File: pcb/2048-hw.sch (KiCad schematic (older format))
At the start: 98 parts, among them J1 UJC-HP-3-SMT-TR, J2 Battery, J3 SWD, SW1 SW_SPDT, SW2 PUSH_A, SW3 PUSH_B, U1 STM32F303K8Tx, U2 MCP73831-2-OT, U3 AP2210N-3.3TRG1, U4 PSP_1000_JSTK, U5 LMV339, Y1 ECS-80-12-30Q-DS-TR

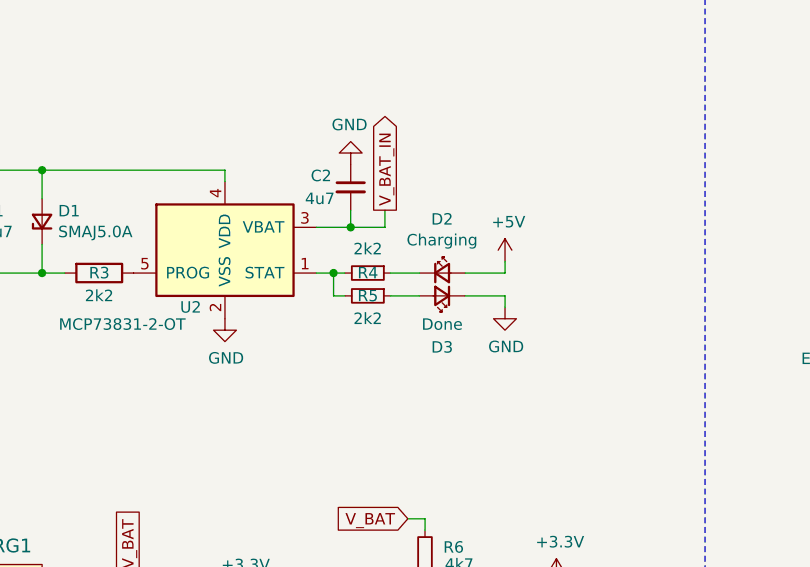
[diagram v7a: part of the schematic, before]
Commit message: Shink down PCB dimensions
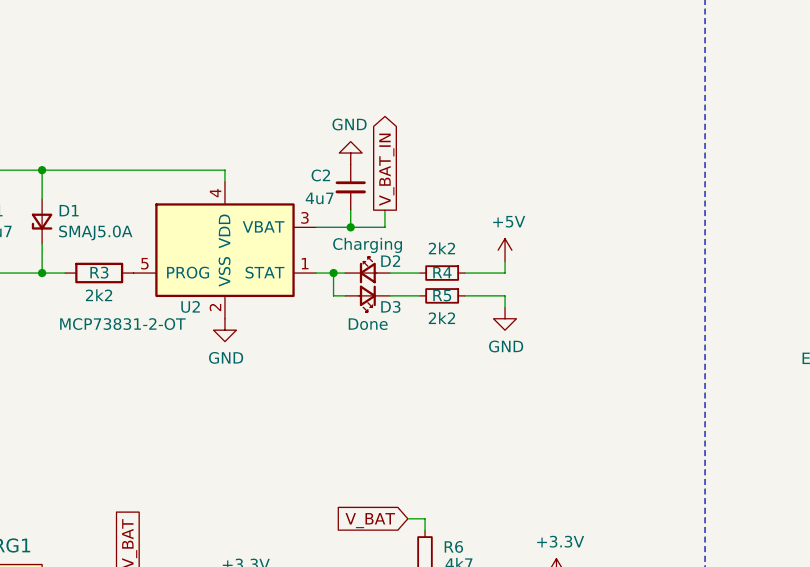
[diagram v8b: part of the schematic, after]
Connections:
- net +5V: now also R4.1; no longer D2.2 (A)
- net GND: now also R5.1; no longer D3.1 (K)
- net at D2.1 (K): now also D3.2 (A), U2.1 (STAT); no longer R4.1
- new net: D2.2 (A), R4.2
- new net: D3.1 (K), R5.2
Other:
- moved on the sheet: D2, D3, R4, R5
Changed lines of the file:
@@
 L Device:LED_Small D2
 U 1 1 5FF0DDA7
-P 5475 1800
-F 0 "D2" H 5475 2035 50  0000 C CNN
-F 1 "Charging" H 5475 1944 50  0000 C CNN
-F 2 "LED_SMD:LED_0603_1608Metric_Pad1.05x0.95mm_HandSolder" V 5475 1800 50  0001 C CNN
-F 3 "~" V 5475 1800 50  0001 C CNN
-	1    5475 1800
+P 5150 1800
+F 0 "D2" H 5250 1850 50  0000 C CNN
+F 1 "Charging" H 5150 1925 50  0000 C CNN
+F 2 "LED_SMD:LED_0603_1608Metric_Pad1.05x0.95mm_HandSolder" V 5150 1800 50  0001 C CNN
+F 3 "~" V 5150 1800 50  0001 C CNN
+	1    5150 1800
 	1    0    0    -1
 $EndComp
@@
 L Device:R_Small R4
 U 1 1 5FF0F744
-P 5150 1800
-F 0 "R4" V 5150 1800 50  0000 C CNN
-F 1 "2k2" V 5045 1800 50  0000 C CNN
-F 2 "Resistor_SMD:R_0603_1608Metric_Pad0.98x0.95mm_HandSolder" H 5150 1800 50  0001 C CNN
-F 3 "~" H 5150 1800 50  0001 C CNN
-	1    5150 1800
+P 5475 1800
+F 0 "R4" V 5475 1800 50  0000 C CNN
+F 1 "2k2" V 5370 1800 50  0000 C CNN
+F 2 "Resistor_SMD:R_0603_1608Metric_Pad0.98x0.95mm_HandSolder" H 5475 1800 50  0001 C CNN
+F 3 "~" H 5475 1800 50  0001 C CNN
+	1    5475 1800
 	0    1    1    0
 $EndComp
@@
 L Device:R_Small R5
 U 1 1 5FF13A07
-P 5150 1900
-F 0 "R5" V 5150 1900 50  0000 C CNN
-F 1 "2k2" V 5250 1900 50  0000 C CNN
-F 2 "Resistor_SMD:R_0603_1608Metric_Pad0.98x0.95mm_HandSolder" H 5150 1900 50  0001 C CNN
-F 3 "~" H 5150 1900 50  0001 C CNN
-	1    5150 1900
+P 5475 1900
+F 0 "R5" V 5475 1900 50  0000 C CNN
+F 1 "2k2" V 5575 1900 50  0000 C CNN
+F 2 "Resistor_SMD:R_0603_1608Metric_Pad0.98x0.95mm_HandSolder" H 5475 1900 50  0001 C CNN
+F 3 "~" H 5475 1900 50  0001 C CNN
+	1    5475 1900
 	0    1    1    0
 $EndComp
@@
 L Device:LED_Small D3
 U 1 1 5FF14086
-P 5475 1900
-F 0 "D3" H 5475 2125 50  0000 C CNN
-F 1 "Done" H 5475 2025 50  0000 C CNN
-F 2 "LED_SMD:LED_0603_1608Metric_Pad1.05x0.95mm_HandSolder" V 5475 1900 50  0001 C CNN
-F 3 "~" V 5475 1900 50  0001 C CNN
-	1    5475 1900
+P 5150 1900
+F 0 "D3" H 5050 1950 50  0000 C CNN
+F 1 "Done" H 5150 2025 50  0000 C CNN
+F 2 "LED_SMD:LED_0603_1608Metric_Pad1.05x0.95mm_HandSolder" V 5150 1900 50  0001 C CNN
+F 3 "~" V 5150 1900 50  0001 C CNN
+	1    5150 1900
 	-1   0    0    1
 $EndComp
